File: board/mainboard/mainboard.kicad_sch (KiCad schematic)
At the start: 31 parts

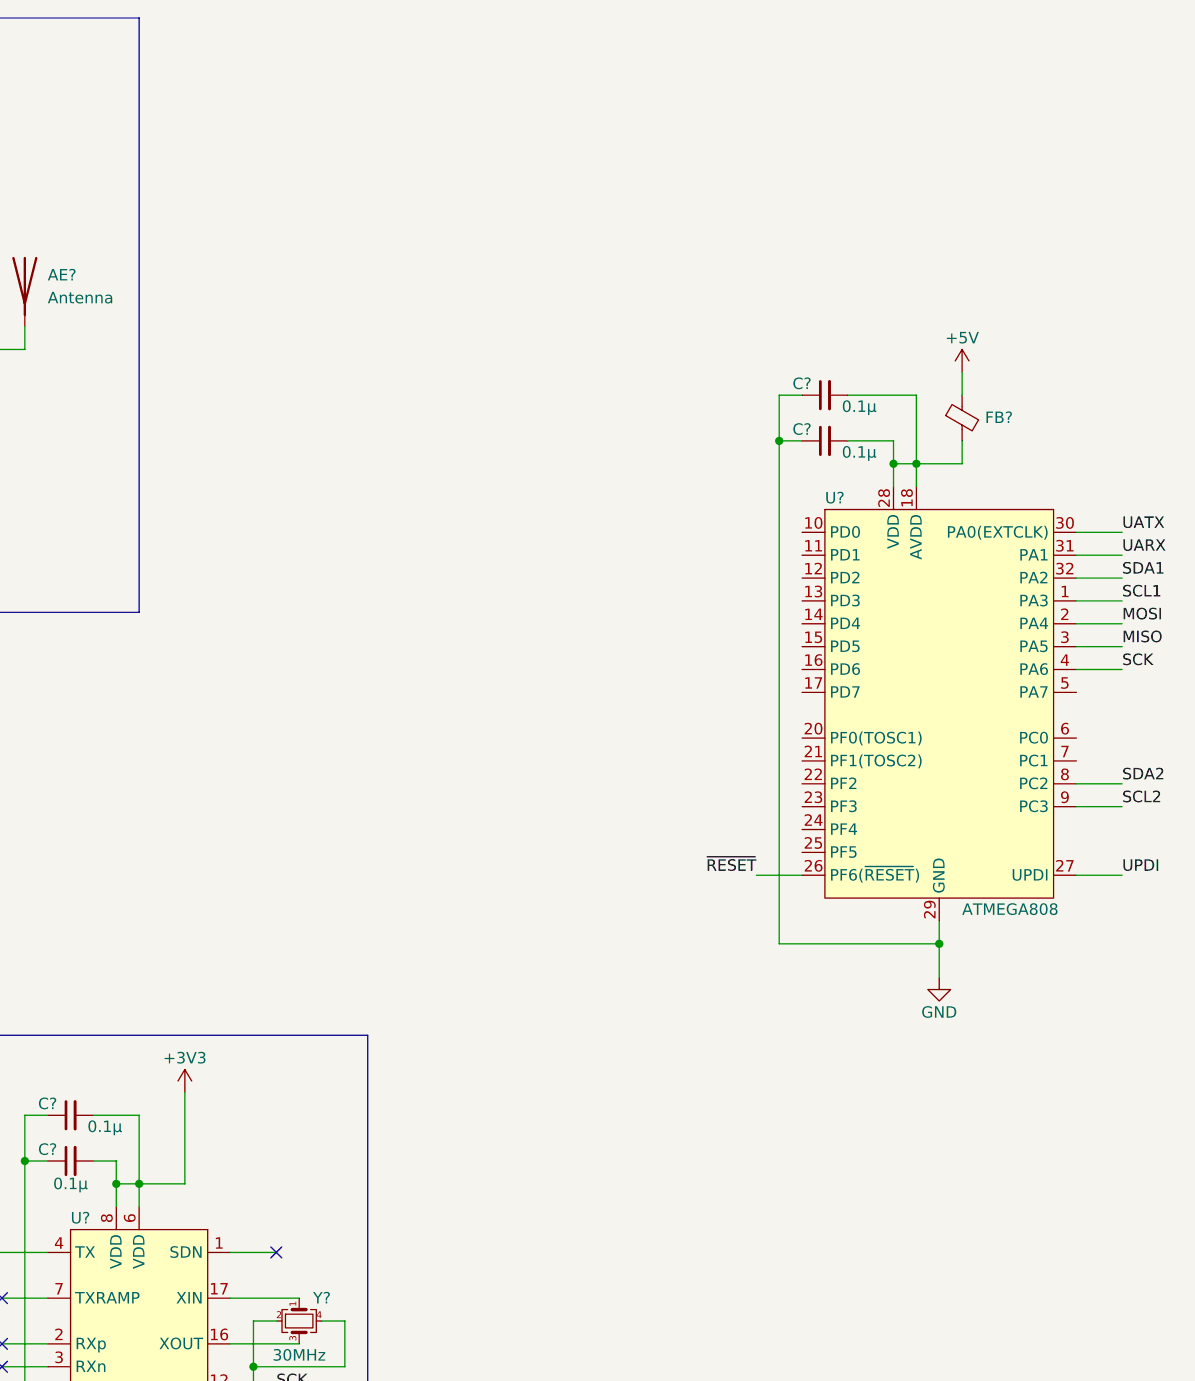
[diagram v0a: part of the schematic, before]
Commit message: added power supply and indicators
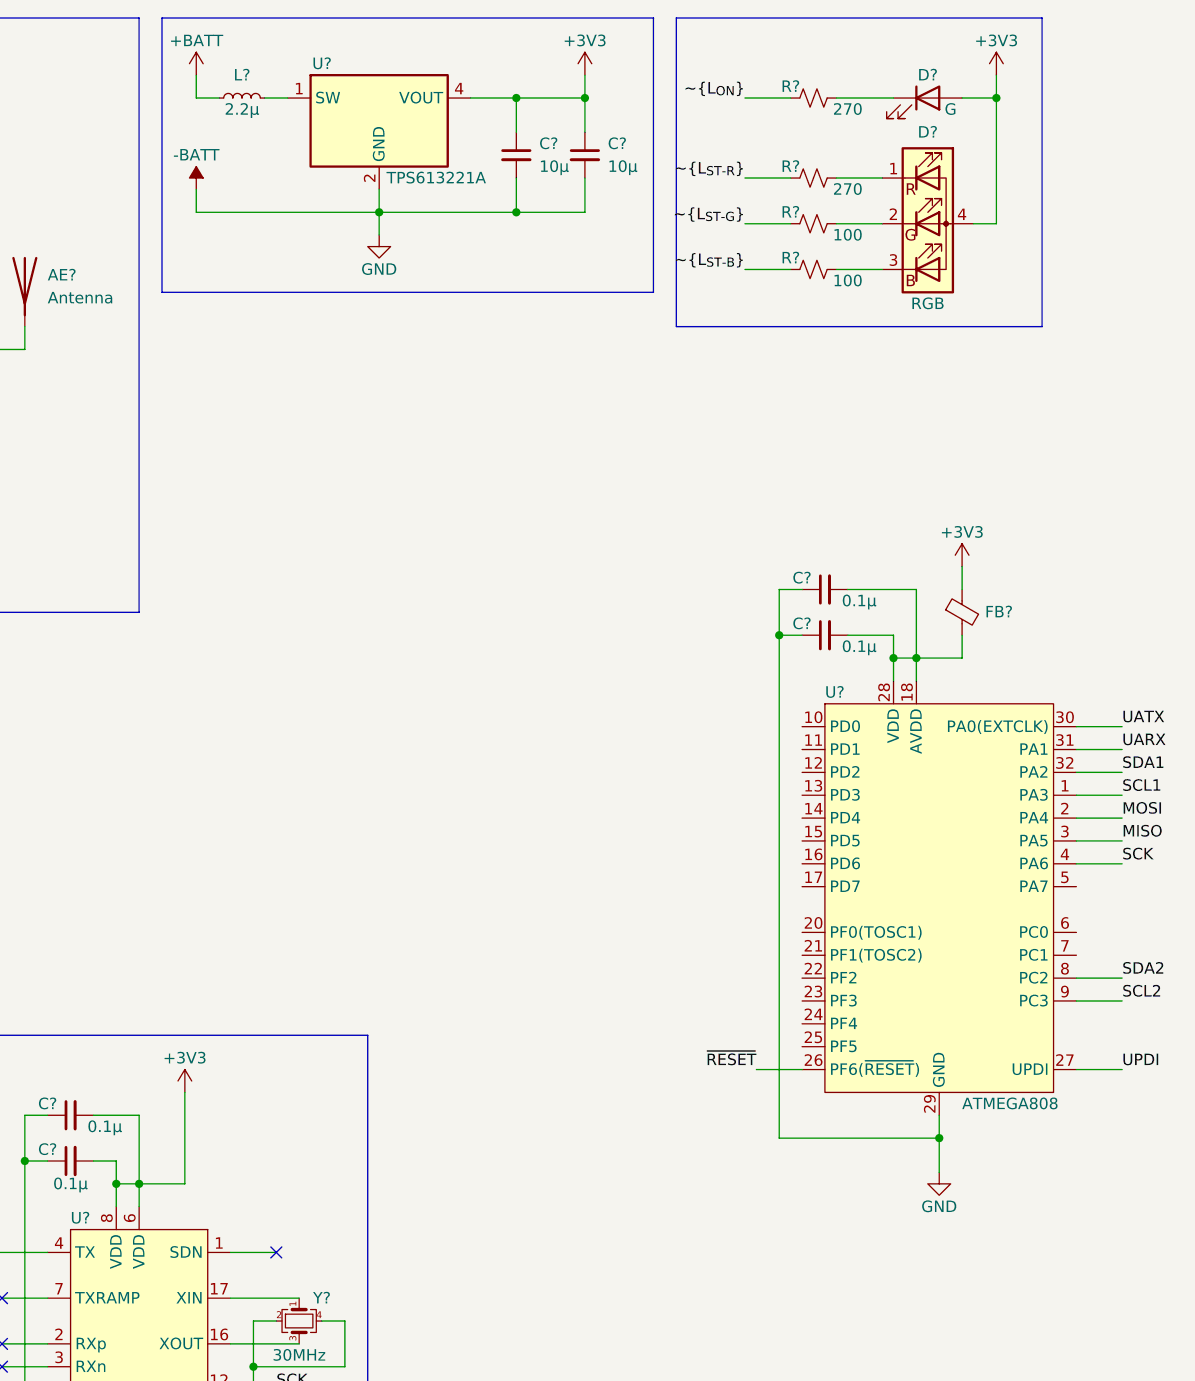
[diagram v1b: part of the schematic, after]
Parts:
- added C? (x2): 10µ, symbol Device:C_Small
- added D?: RGB, symbol Device:LED_RGBA
- added D?: G, symbol Device:LED
- added L?: 2.2µ, symbol Device:L_Small
- added R? (x2): 270, symbol Device:R_Small_US
- added R? (x2): 100, symbol Device:R_Small_US
- added U?: TPS613221A, Package_TO_SOT_SMD:SOT-23-5, symbol Regulator_Switching:TPS613221ADBV
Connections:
- net +3V3: now also FB?.1, C?.1, C?.1, D?.2 (A), D?.4 (A), U?.4 (VOUT)
- net +5V: no longer FB?.1
- net GND renamed -BATT
- net -BATT: now also C?.2, C?.2, U?.2 (GND)
- new net: D?.1 (RK), R?.2
- new net: D?.2 (GK), R?.2
- new net: D?.3 (BK), R?.2
- new net: D?.1 (K), R?.2
- new net: L?.2, U?.1 (SW)
- new net +BATT: L?.1
- new net ~{L_{ON}}: R?.1
- new net ~{L_{ST-B}}: R?.1
- new net ~{L_{ST-G}}: R?.1
- new net ~{L_{ST-R}}: R?.1
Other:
- moved on the sheet: C?, FB?, U?

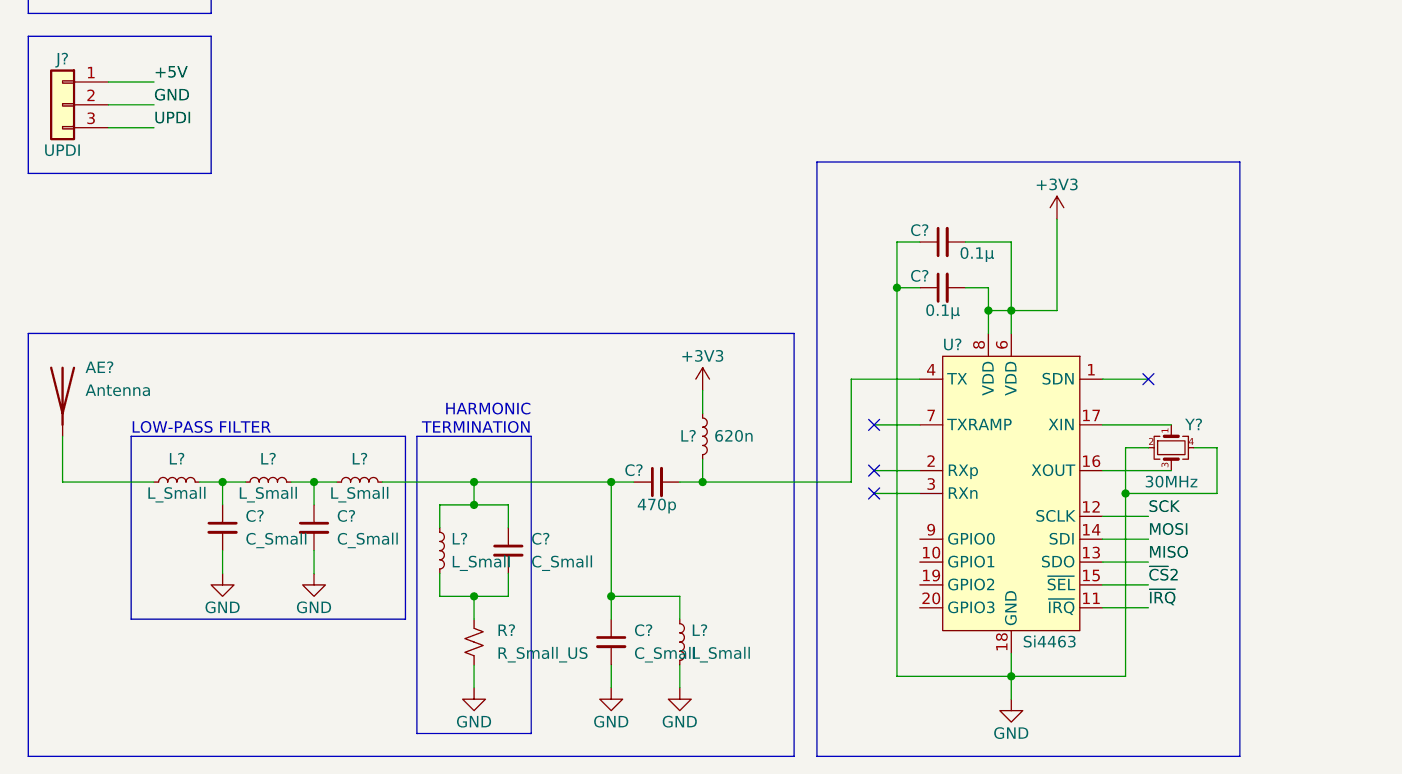
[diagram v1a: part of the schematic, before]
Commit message: added tx filter circuit values
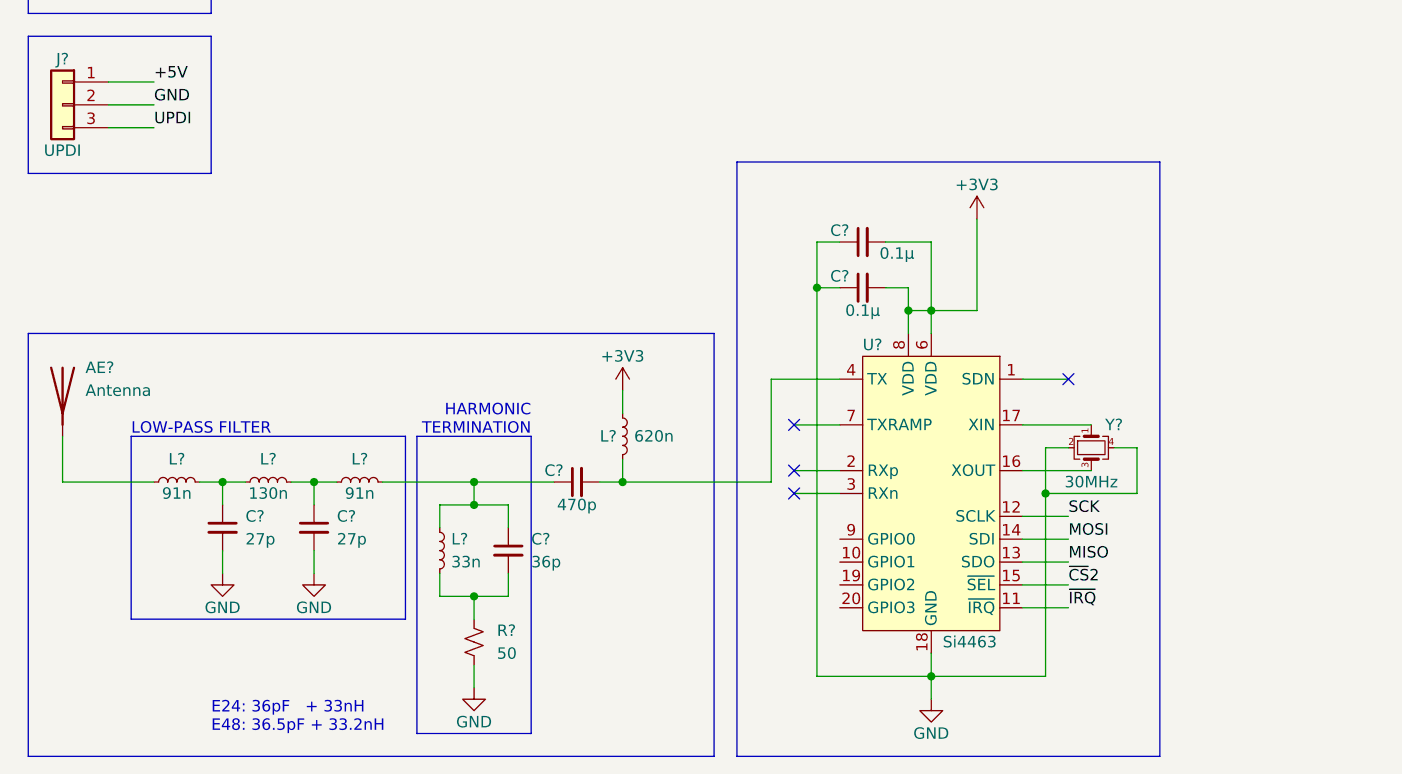
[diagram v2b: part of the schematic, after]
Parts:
- removed C?: C_Small, symbol Device:C_Small
- removed L?: L_Small, symbol Device:L_Small
- C?: value C_Small -> 36p
- C? (x2): value C_Small -> 27p
- D?: footprint (none) -> LED_SMD:LED_LiteOn_LTST-C19HE1WT
- D?: footprint (none) -> LED_SMD:LED_0603_1608Metric_Pad1.05x0.95mm_HandSolder
- L? (x2): value L_Small -> 91n
- L?: value L_Small -> 130n
- L?: value L_Small -> 33n
- R?: value R_Small_US -> 50
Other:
- note added: "E24: 36pF + 33nH E48: 36.5pF + 33.2nH"
- moved on the sheet: C?, L?, U?, Y?

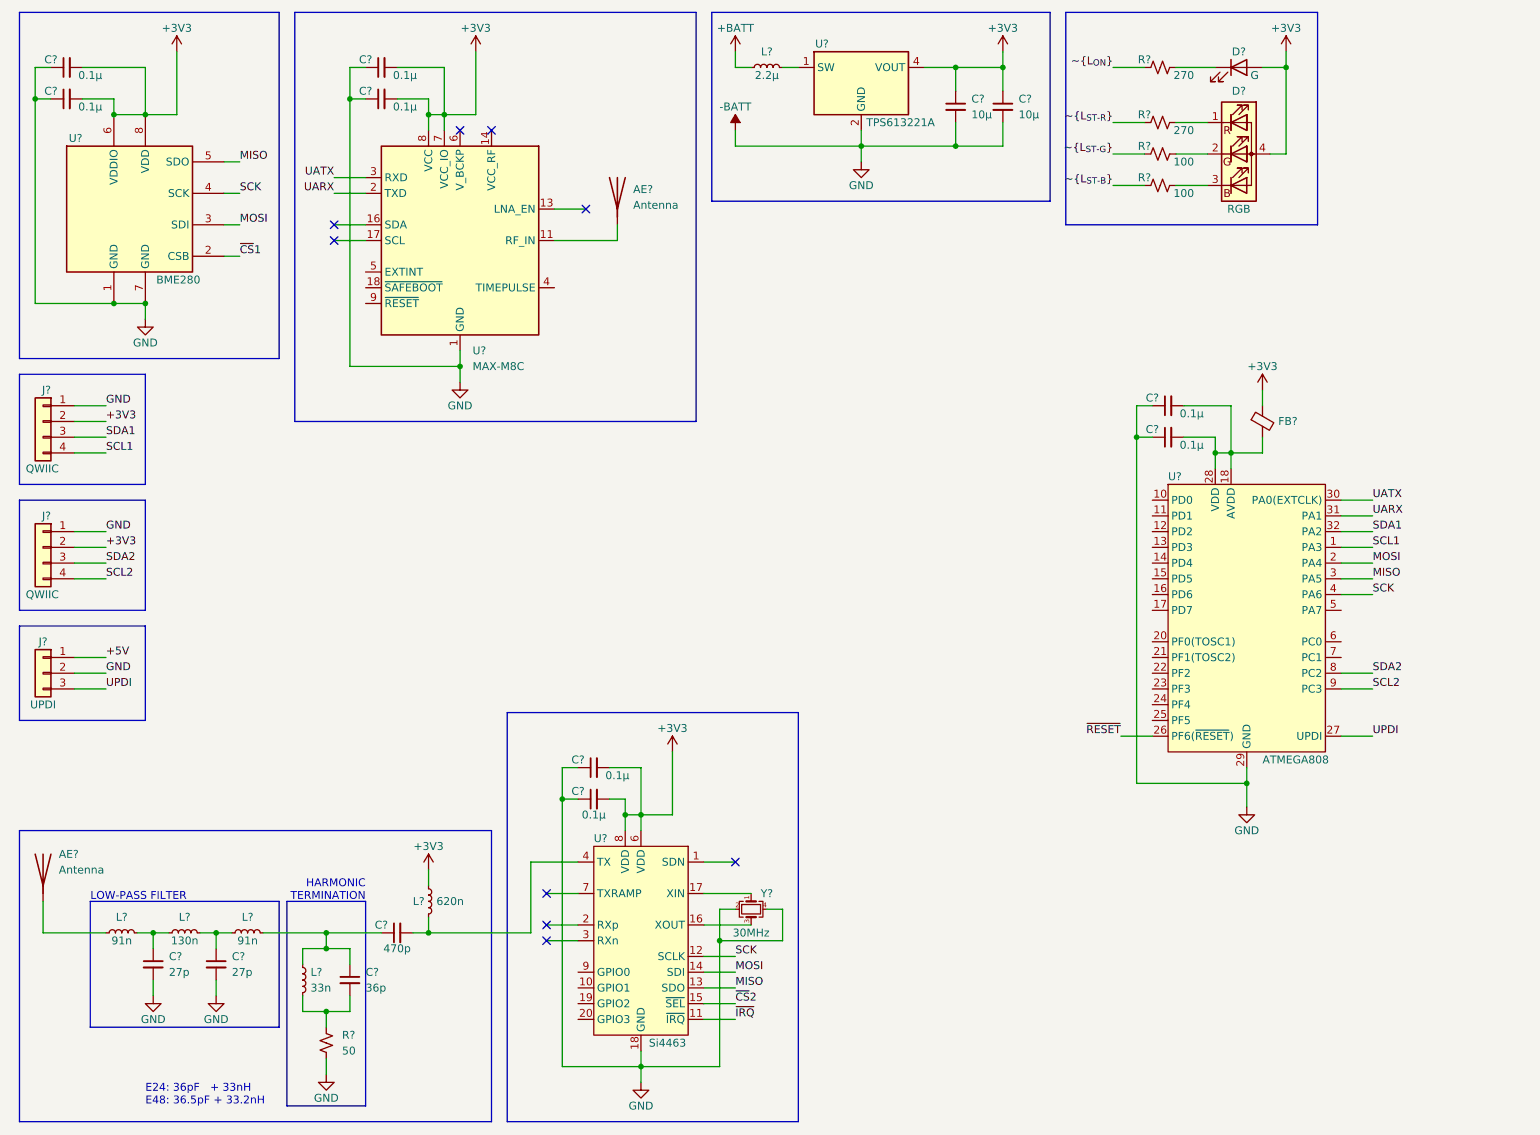
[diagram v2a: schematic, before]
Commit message: added designation and footprint to (most) components
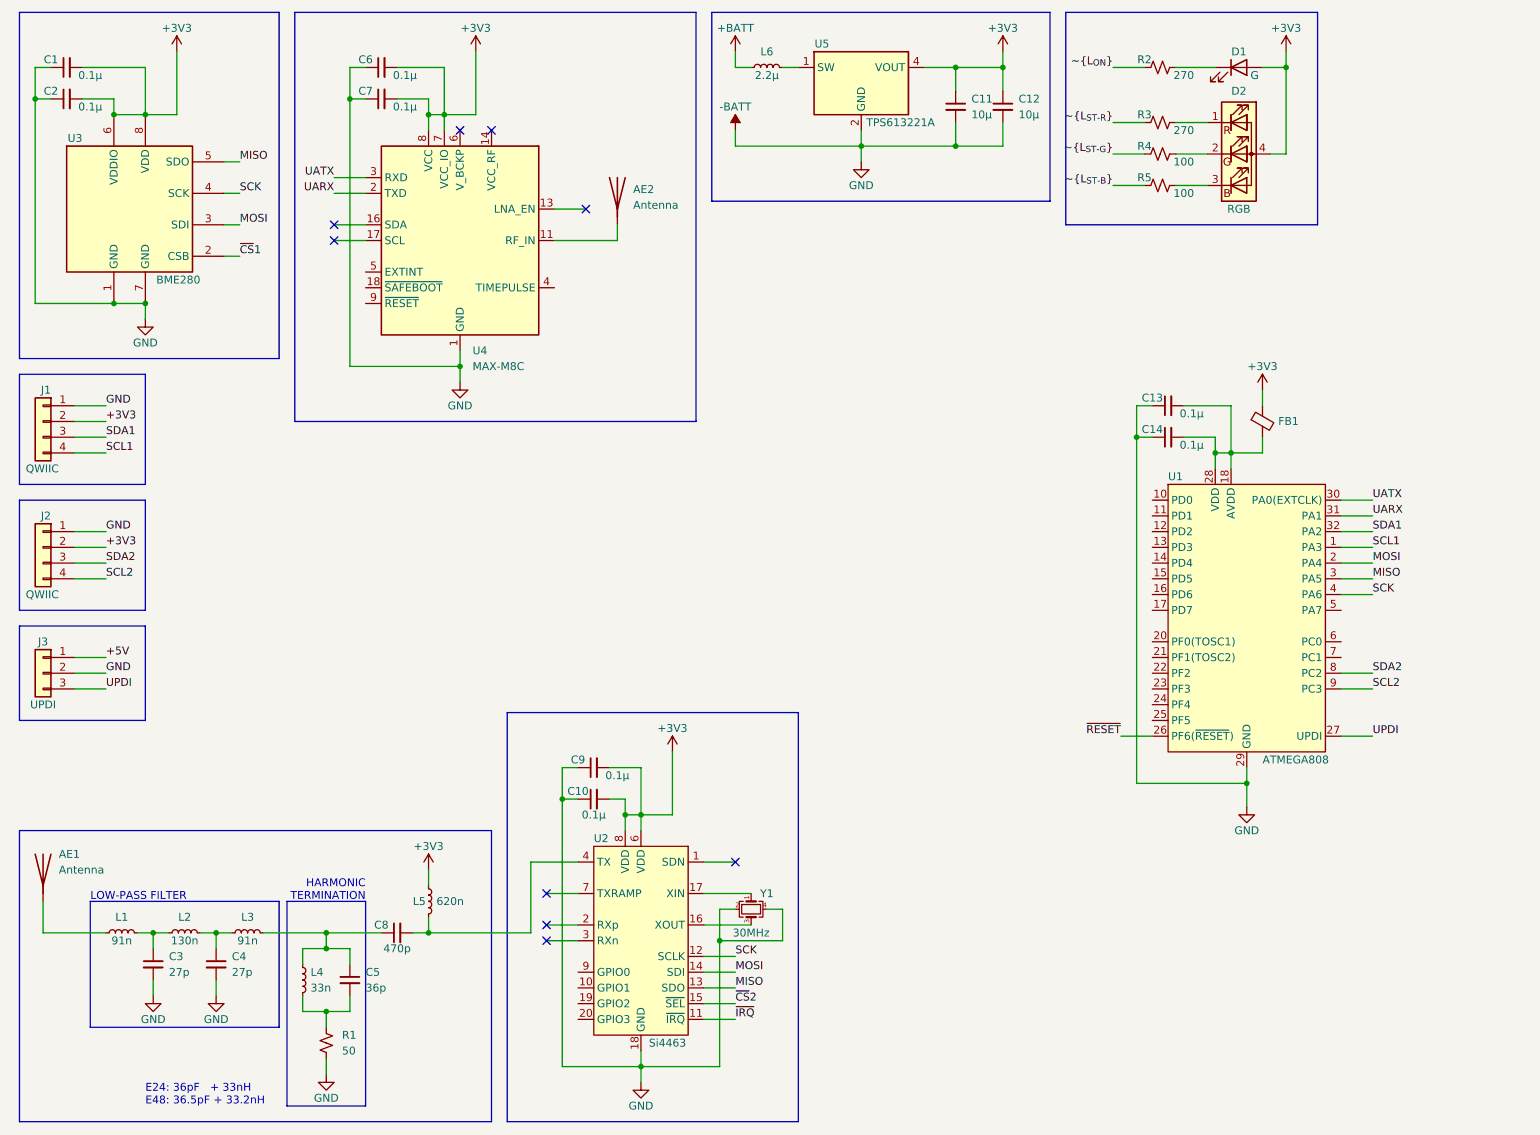
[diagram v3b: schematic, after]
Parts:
- C1, C10, C13, C14, C2, C3, C4, C5, C6, C7, C8, C9: renamed from C?; footprint (none) -> Capacitor_SMD:C_0603_1608Metric_Pad1.08x0.95mm_HandSolder
- C11, C12: renamed from C?; footprint (none) -> Capacitor_SMD:C_0805_2012Metric_Pad1.18x1.45mm_HandSolder
- L1, L2, L3, L4: renamed from L?; footprint (none) -> Inductor_SMD:L_0603_1608Metric_Pad1.05x0.95mm_HandSolder
- L5: renamed from L?; footprint (none) -> Inductor_SMD:L_1008_2520Metric_Pad1.43x2.20mm_HandSolder
- L6: renamed from L?; footprint (none) -> Inductor_SMD:L_0805_2012Metric_Pad1.15x1.40mm_HandSolder
- R1, R2, R3, R4, R5: renamed from R?; footprint (none) -> Resistor_SMD:R_0603_1608Metric_Pad0.98x0.95mm_HandSolder
- gave numbers to parts that had none: 14

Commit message: latest PCB design update (will commit better henceforth)
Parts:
- removed AE1, AE2: Antenna, symbol Device:Antenna
- added AE1: Antenna_Dipole, Dipole:AE_Pad, symbol Device:Antenna_Dipole
- added AE2: 1575AT54A0100, 1575AT54:Johanson_AT54, symbol 1575AT54:1575AT54A0100
- added BT1: AAA, Battery:BatteryHolder_Keystone_2466_1xAAA, symbol Device:Battery_Cell
- added H1: M2, MountingHole:MountingHole_2.2mm_M2, symbol Mechanical:MountingHole
- added J4: RFShield_OnePiece, RF_Shielding:Wuerth_36103205_20x20mm, symbol Device:RFShield_OnePiece
- added SW1: SAJ1-SNC, SAJ13:SAJ1______N88SNCPT_, symbol Switch:SW_Push_Open
- C1, C10, C13, C14, C2, C6, C7, C9: footprint Capacitor_SMD:C_0603_1608Metric_Pad1.08x0.95mm_HandSolder -> Capacitor_SMD:C_0402_1005Metric
- C11, C12: footprint Capacitor_SMD:C_0805_2012Metric_Pad1.18x1.45mm_HandSolder -> Capacitor_SMD:C_0603_1608Metric
- C3, C4, C5, C8: footprint Capacitor_SMD:C_0603_1608Metric_Pad1.08x0.95mm_HandSolder -> Capacitor_SMD:C_0603_1608Metric
- D1: footprint LED_SMD:LED_0603_1608Metric_Pad1.05x0.95mm_HandSolder -> LED_SMD:LED_0603_1608Metric
- FB1: footprint Inductor_SMD:L_0805_2012Metric_Pad1.05x1.20mm_HandSolder -> Inductor_SMD:L_0805_2012Metric
- J3: footprint Connector_PinHeader_2.54mm:PinHeader_1x03_P2.54mm_Vertical -> Connector_PinHeader_2.54mm:PinHeader_1x03_P2.54mm_Horizontal
- L1, L2, L3, L4: footprint Inductor_SMD:L_0603_1608Metric_Pad1.05x0.95mm_HandSolder -> Inductor_SMD:L_0603_1608Metric
- L5: value 620n -> 390n; footprint Inductor_SMD:L_1008_2520Metric_Pad1.43x2.20mm_HandSolder -> Inductor_SMD:L_0603_1608Metric
- R1, R2, R3, R4, R5: footprint Resistor_SMD:R_0603_1608Metric_Pad0.98x0.95mm_HandSolder -> Resistor_SMD:R_0603_1608Metric
- Y1: footprint (none) -> Crystal:Crystal_SMD_3225-4Pin_3.2x2.5mm
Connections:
- net at L1.1: now also AE1.2
- net at U4.11 (RF_IN): now also AE2.1 (RF)
- net +BATT: no longer names the net of L6.1
- net +BATT: now also SW1.1 (A)
- net -BATT renamed GND
- net GND: now also AE1.1, AE2.2 (GND), AE2.4 (GND), BT1.2 (-), J4.1 (Shield)
- new net: BT1.1 (+), SW1.2 (B)
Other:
- moved on the sheet: C10, C11, C12, C3, C4, C5, C8, C9, D1, D2, L1, L2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
